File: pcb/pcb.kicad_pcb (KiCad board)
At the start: 2 copper layers, 299.5 x 113.5 mm, 430 parts, among them J2 Conn_02x05_Odd_Even, M1 Ezurio BL54L15 (nrf54L15) mod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, SW1 SW_DIP_x01

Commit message: M  pcb/pcb.kicad_pcb M  pcb/pcb.kicad_prl
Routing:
- net /SW0: track 276.5 -> 1002.0 mm, vias 7 -> 26
- net /SW1: track 391.0 -> 714.2 mm, vias 12 -> 27
- net /SW2: track 309.0 -> 460.9 mm, vias 17 -> 21
- net /SW3: track 329.3 -> 448.4 mm, vias 16 -> 29
- net /CS7: track 186.6 -> 191.3 mm
- net /ANA_69: track 80.9 -> 82.8 mm
- net VCCS: track 2253.4 -> 2254.7 mm
- net /ANA_70: track 86.3 -> 86.8 mm
- net /ANA_56: track 65.3 -> 65.9 mm
- net /ANA_71: track 103.0 -> 103.5 mm
- net /CS8: track 124.4 -> 124.9 mm

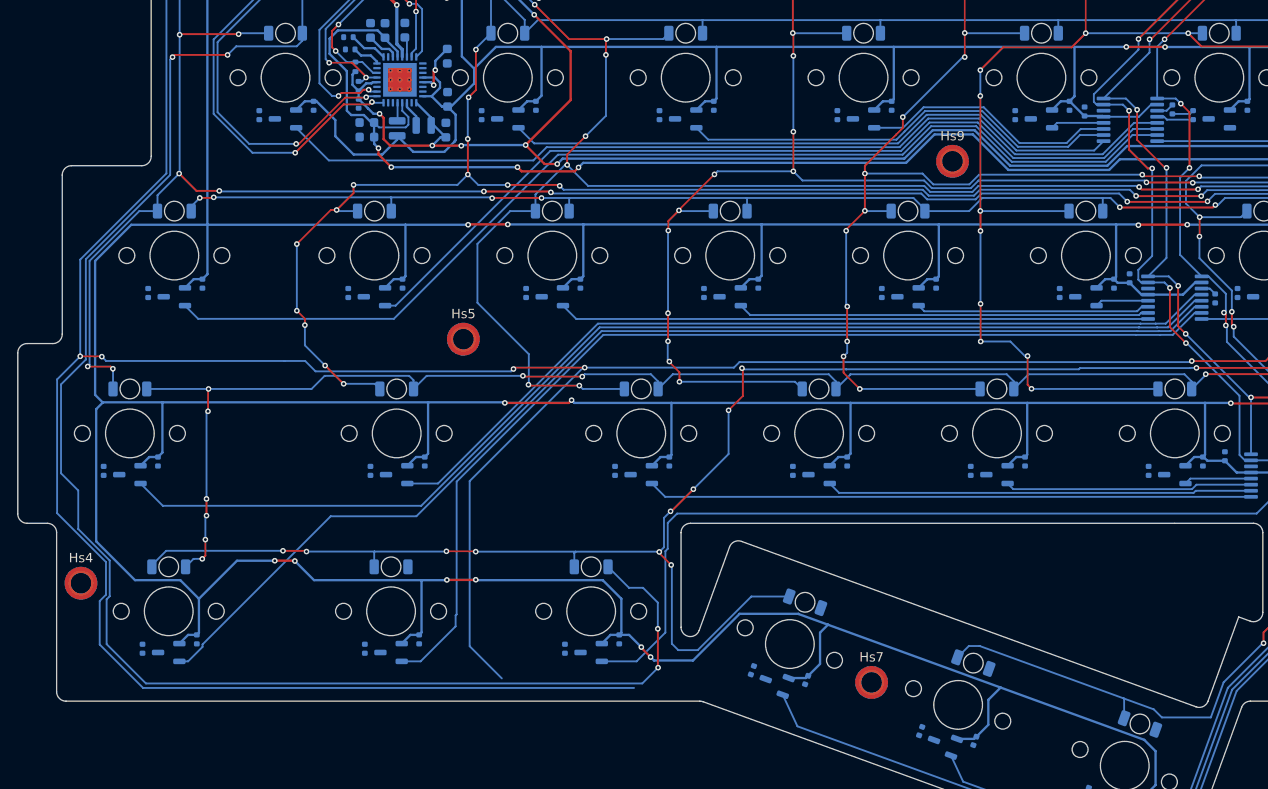
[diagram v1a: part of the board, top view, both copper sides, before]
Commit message: M  pcb/pcb.kicad_pcb M  pcb/pcb.kicad_prl
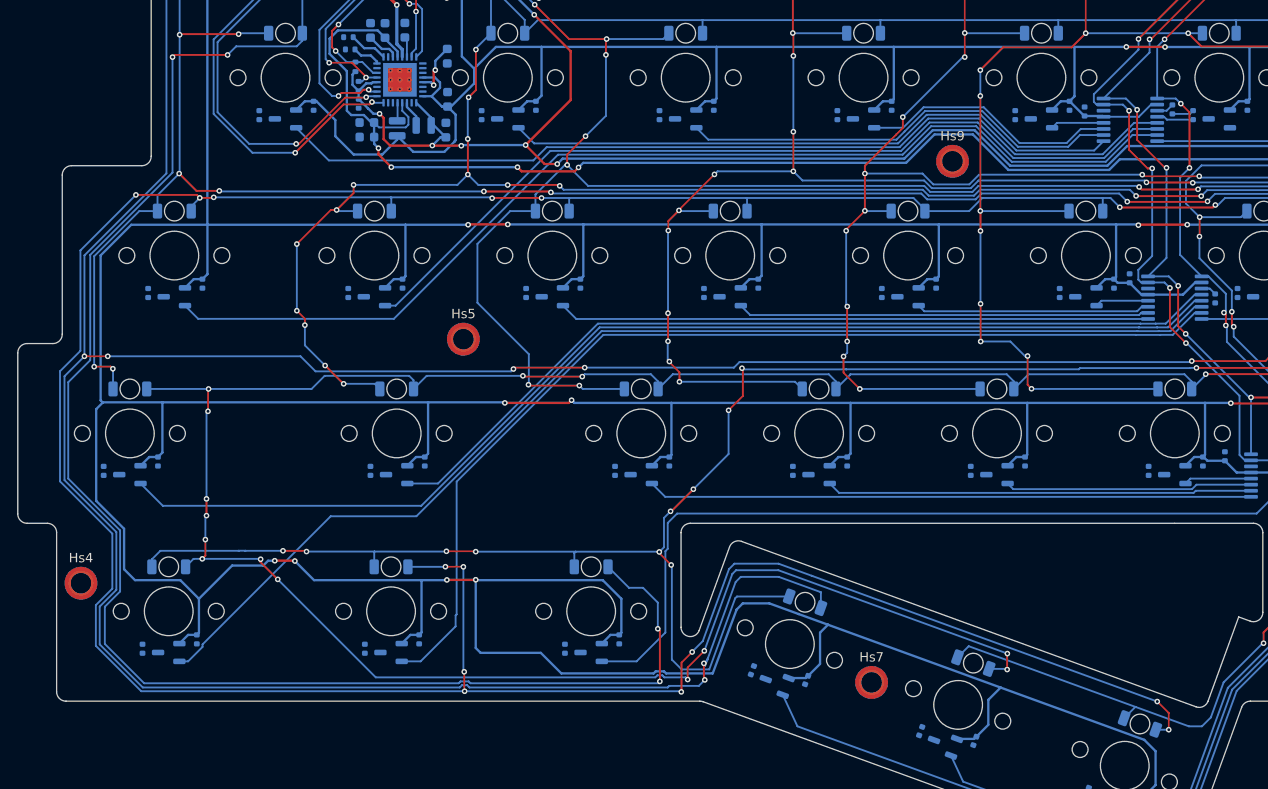
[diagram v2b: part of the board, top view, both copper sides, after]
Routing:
- net /SW2: track 460.9 -> 674.4 mm, vias 21 -> 30
- net /SW3: track 448.4 -> 553.3 mm, vias 29 -> 35
- net VCCS: track 2254.7 -> 2280.1 mm, vias 44 -> 42
- net /SW0: track 1002.0 -> 993.6 mm, vias 26 -> 28
- net /CS9: track 182.3 -> 187.6 mm
- net /SW1: track 714.2 -> 716.0 mm
- net /CS10: track 203.2 -> 202.3 mm

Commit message: M  pcb/pcb.kicad_pcb M  pcb/pcb.kicad_prl M  pcb/pcb.kicad_sch M  pcb/switch.kicad_sch M  placefp.py A  tmr-footprints/Button_Switch_3x4x2.5.kicad_mod A  tmr-footprints/Panasonic_EVPAE.kicad_mod
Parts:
- added JTAG2: Conn_02x05_Odd_Even, Connector:Tag-Connect_TC2050-IDC-FP_2x05_P1.27mm_Vertical, F.Cu at (67.1, -14.9)
- BAT1: value Battery_Pack_PS5 -> ~; footprint Connector_JST:JST_EH_S3B-EH_1x03_P2.50mm_Horizontal -> Connector_JST:JST_SH_BM03B-SRSS-TB_1x03-1MP_P1.00mm_Vertical
- SW1: footprint Button_Switch_SMD:SW_SPST_Omron_B3FS-105xP -> tmr-lib:Button_Switch_3x4x2.5; moved to B.Cu
- moved Hs12 304.6 mm to (255.2, 38.0)
- moved JLC1 223.7 mm to (48.6, 66.0), turned to 0 degrees
- moved BAT1 102.6 mm to (25.0, 83.0), turned to 180 degrees
- moved SW1 52.9 mm to (21.0, 38.0), turned to -90 degrees
- moved USB1 29.7 mm to (12.8, 19.0), turned to -90 degrees
- moved C15 29.0 mm to (19.3, 27.1)
- moved JTAG1 19.3 mm to (27.5, -4.89), turned to 0 degrees
- moved R3 9.31 mm to (31.9, 23.9), turned to 90 degrees
- moved C28 9.04 mm to (29.4, 22.3), turned to 180 degrees
- moved C21 9.00 mm to (41.7, 15.6)
- moved C7 8.79 mm to (40.7, 22.3), turned to -90 degrees
- moved L2 8.77 mm to (39.9, 16.7), turned to -90 degrees
- moved C22 8.63 mm to (36.5, 14.0), turned to 180 degrees
- moved C8 8.45 mm to (29.4, 20.8), turned to 180 degrees
- moved C23 8.36 mm to (33.1, 14.1), turned to 0 degrees
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- renumbered C6 to C1, C15 to C10, C16 to C11, C17 to C12, C18 to C13, C5 to C14, C7 to C15, C20 to C16, C21 to C17, C22 to C18, C23 to C19, C8 to C2, C24 to C20, C12 to C21, C13 to C22, C14 to C23, C27 to C24, C28 to C25, C29 to C26, C30 to C27, C19 to C28, C25 to C29, C9 to C3, C26 to C30, C10 to C4, C11 to C5, C1 to C6, C2 to C7, C3 to C8, C4 to C9, J2 to JTAG1
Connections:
- C22 pad 1: VCCS -> /VOUT2
- C23 pad 1: /VCC_tmr -> VCCS
- L2 pad 1: VCCS -> /VOUT2
- PMIC1 pad 28: VCCS -> /VOUT2
- PMIC1 pad 29: /VCC_tmr -> VCCS
- PMIC1 pad 32: VCCS -> /VOUT2
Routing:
- net /VDDIO: track 334.3 -> 231.8 mm, vias 12 -> 7
- net Net-(BAT1-NTC): track 0.00 -> 70.8 mm, vias 0 -> 7
- net Net-(BAT1-VBAT): track 3.51 -> 67.4 mm, vias 0 -> 5
- net VCCS: track 2280.1 -> 2241.1 mm, vias 42 -> 44
- net Net-(PMIC1-SHPHLD): track 0.00 -> 28.9 mm, vias 0 -> 4
- net /SWDIO: track 111.1 -> 134.7 mm
- net /SWDCLK: track 113.4 -> 133.8 mm
- net /VOUT2: track 0.00 -> 19.3 mm
- net /INT: track 193.1 -> 210.7 mm
- net /LOADSW_CTRL: track 188.6 -> 205.7 mm
- net GND: track 41.0 -> 53.3 mm
- net /NRESET: track 117.6 -> 129.4 mm
- net Net-(PMIC1-SW2): track 1.95 -> 13.7 mm
- net /SCL: track 172.2 -> 179.9 mm
- net /VSYS: track 160.8 -> 153.1 mm
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
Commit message: M  pcb/pcb.kicad_pcb M  pcb/pcb.kicad_sch A  tmr-footprints/MountingHole_2.2mm_M2_ISO7380_Pad_TopBottom.kicad_mod
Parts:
- Hs1, Hs10, Hs11, Hs12, Hs2, Hs3, Hs4, Hs5, Hs6, Hs7, Hs8, Hs9: footprint MountingHole:MountingHole_2.2mm_M2_ISO7380_Pad_TopBottom -> tmr-lib:MountingHole_2.2mm_M2_ISO7380_Pad_TopBottom
- JTAG2: footprint Connector:Tag-Connect_TC2050-IDC-FP_2x05_P1.27mm_Vertical -> Connector:Tag-Connect_TC2050-IDC-NL_2x05_P1.27mm_Vertical; moved to B.Cu
- moved JTAG2 59.3 mm to (11.8, 6.75), turned to -90 degrees
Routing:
- net /SWDCLK: track 133.8 -> 165.8 mm, vias 0 -> 4
- net /NRESET: track 129.4 -> 160.4 mm, vias 0 -> 2
- net /SWDIO: track 134.7 -> 159.4 mm, vias 0 -> 2
- net /VDDIO: track 231.8 -> 255.0 mm
- net GND: track 53.3 -> 58.6 mm
- net /SW0: track 995.1 -> 997.0 mm
